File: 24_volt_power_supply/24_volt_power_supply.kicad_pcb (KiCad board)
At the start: 2 copper layers, 75 x 55 mm, 16 parts, among them J1 Conn_01x02_Pin, J2 Screw_Terminal_01x02, J3 Conn_01x02_Pin, J4 Conn_01x03_Pin, K1 Relay_SPDT

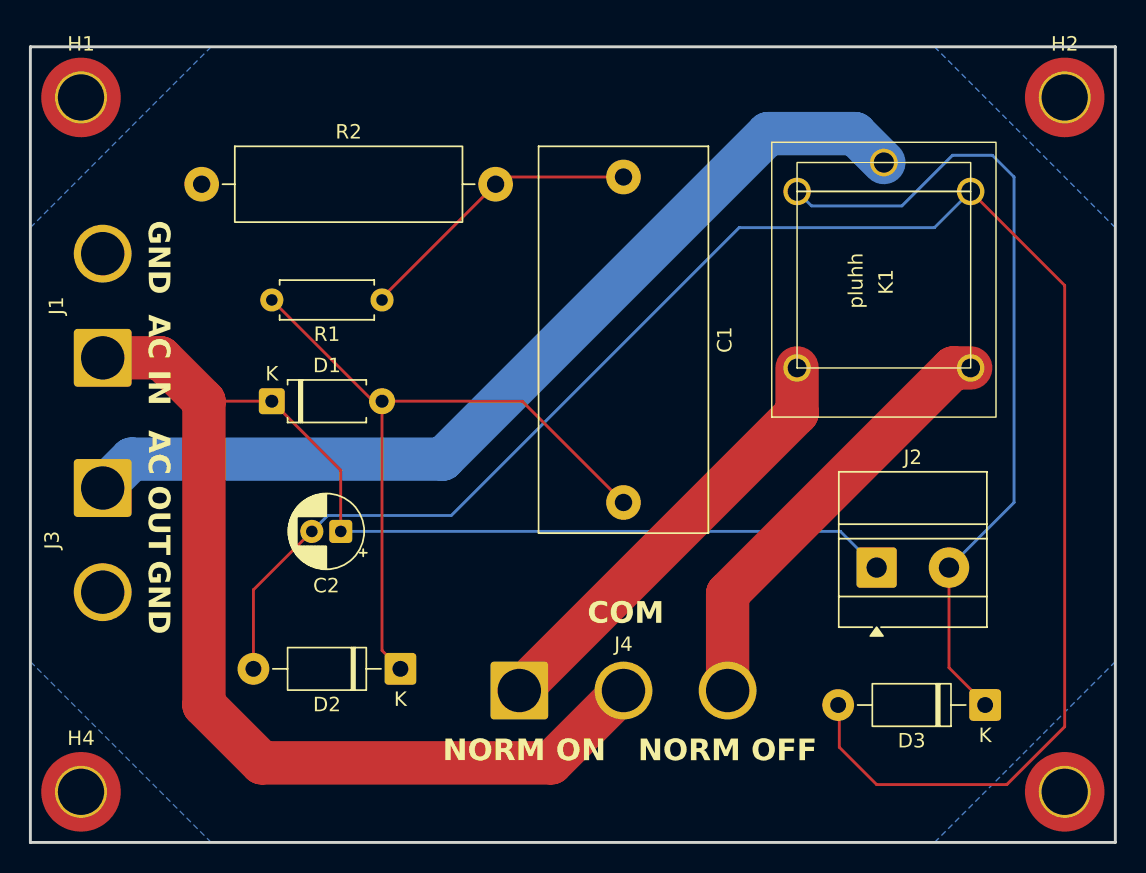
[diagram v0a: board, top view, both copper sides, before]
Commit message: fixed spacing for trace and mounting hole. NEED TO FIX LIVE WIRE TRACES, TOO THIN
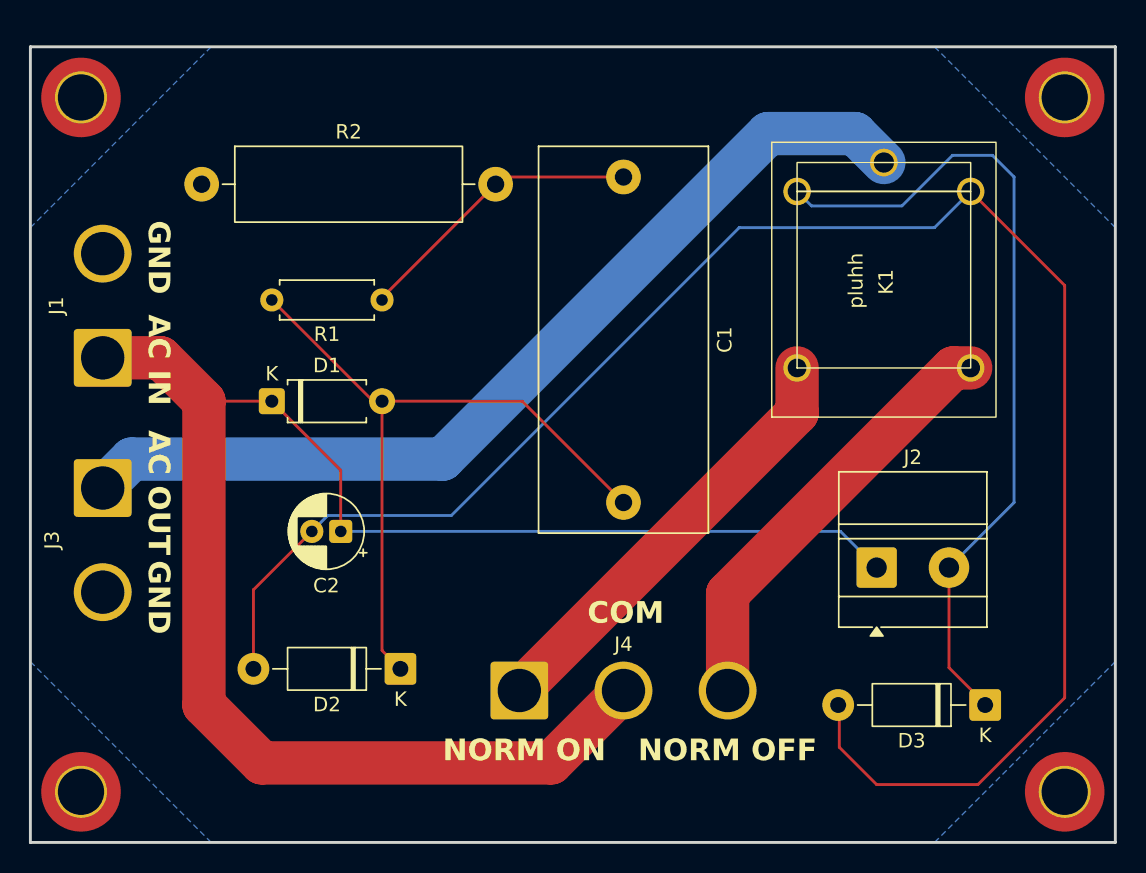
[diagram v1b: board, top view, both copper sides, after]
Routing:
- net Net-(D2-A): track 127.4 -> 126.2 mm
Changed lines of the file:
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@@
 		(tags "mountinghole M3 ISO14580")
 		(property "Reference" "H1"
-			(at 0 -3.7 0)
-			(layer "F.SilkS")
+			(at 0 -6 0)
+			(layer "F.Fab")
 			(effects
 				(font
@@
 		)
 		(property "Value" "MountingHole"
-			(at 0 3.7 0)
+			(at 0 -8 0)
 			(layer "F.Fab")
 			(effects
@@
 		(tags "mountinghole M3 ISO14580")
 		(property "Reference" "H2"
-			(at 0 -3.7 0)
-			(layer "F.SilkS")
+			(at 0 -6.5 0)
+			(layer "F.Fab")
 			(effects
 				(font
@@
 		)
 		(property "Value" "MountingHole"
-			(at 0 3.7 0)
+			(at 0 -8.5 0)
 			(layer "F.Fab")
 			(effects
@@
 		(tags "mountinghole M3 ISO14580")
 		(property "Reference" "H3"
-			(at 0 6.5 0)
+			(at 0 7 0)
 			(layer "F.Fab")
 			(effects
@@
 		)
 		(property "Value" "MountingHole"
-			(at 0 4.5 0)
+			(at 0 5 0)
 			(layer "F.Fab")
 			(effects
@@
 		(tags "mountinghole M3 ISO14580")
 		(property "Reference" "H4"
-			(at 0 -3.7 0)
-			(layer "F.SilkS")
+			(at 0 7.5 0)
+			(layer "F.Fab")
 			(effects
 				(font
@@
 		)
 		(property "Value" "MountingHole"
-			(at 0 5 0)
+			(at 0 5.5 0)
 			(layer "F.Fab")
 			(effects
@@
 	)
 	(segment
-		(start 127.42 98.42)
-		(end 130 101)
+		(start 143 66.5)
+		(end 136.5 60)
 		(width 0.2)
 		(layer "F.Cu")
@@
 	)
 	(segment
-		(start 127.42 95.5)
-		(end 127.42 98.42)
+		(start 143 95)
+		(end 143 66.5)
 		(width 0.2)
 		(layer "F.Cu")
@@
 	)
 	(segment
-		(start 139 101)
-		(end 143 97)
+		(start 127.42 98.42)
+		(end 130 101)
 		(width 0.2)
 		(layer "F.Cu")
@@
 	)
 	(segment
-		(start 143 97)
-		(end 143 66.5)
+		(start 130 101)
+		(end 137 101)
 		(width 0.2)
 		(layer "F.Cu")
@@
 	)
 	(segment
-		(start 86.92 93)
-		(end 86.92 87.535113)
+		(start 127.42 95.5)
+		(end 127.42 98.42)
 		(width 0.2)
 		(layer "F.Cu")
@@
 	)
 	(segment
-		(start 143 66.5)
-		(end 136.5 60)
+		(start 86.92 93)
+		(end 86.92 87.535113)
 		(width 0.2)
 		(layer "F.Cu")
@@
 	)
 	(segment
-		(start 86.92 87.535113)
-		(end 90.955113 83.5)
+		(start 137 101)
+		(end 143 95)
 		(width 0.2)
 		(layer "F.Cu")
@@
 	)
 	(segment
-		(start 130 101)
-		(end 139 101)
+		(start 86.92 87.535113)
+		(end 90.955113 83.5)
 		(width 0.2)
 		(layer "F.Cu")
